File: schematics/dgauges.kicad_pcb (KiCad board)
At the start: 2 copper layers, 116 x 53.9 mm, 21 parts, among them J1 Conn_01x05_Female, U1 74HC595N, U2 74HC595N, U3 74HC595N, U4 74HC595N, U5 74HC595N

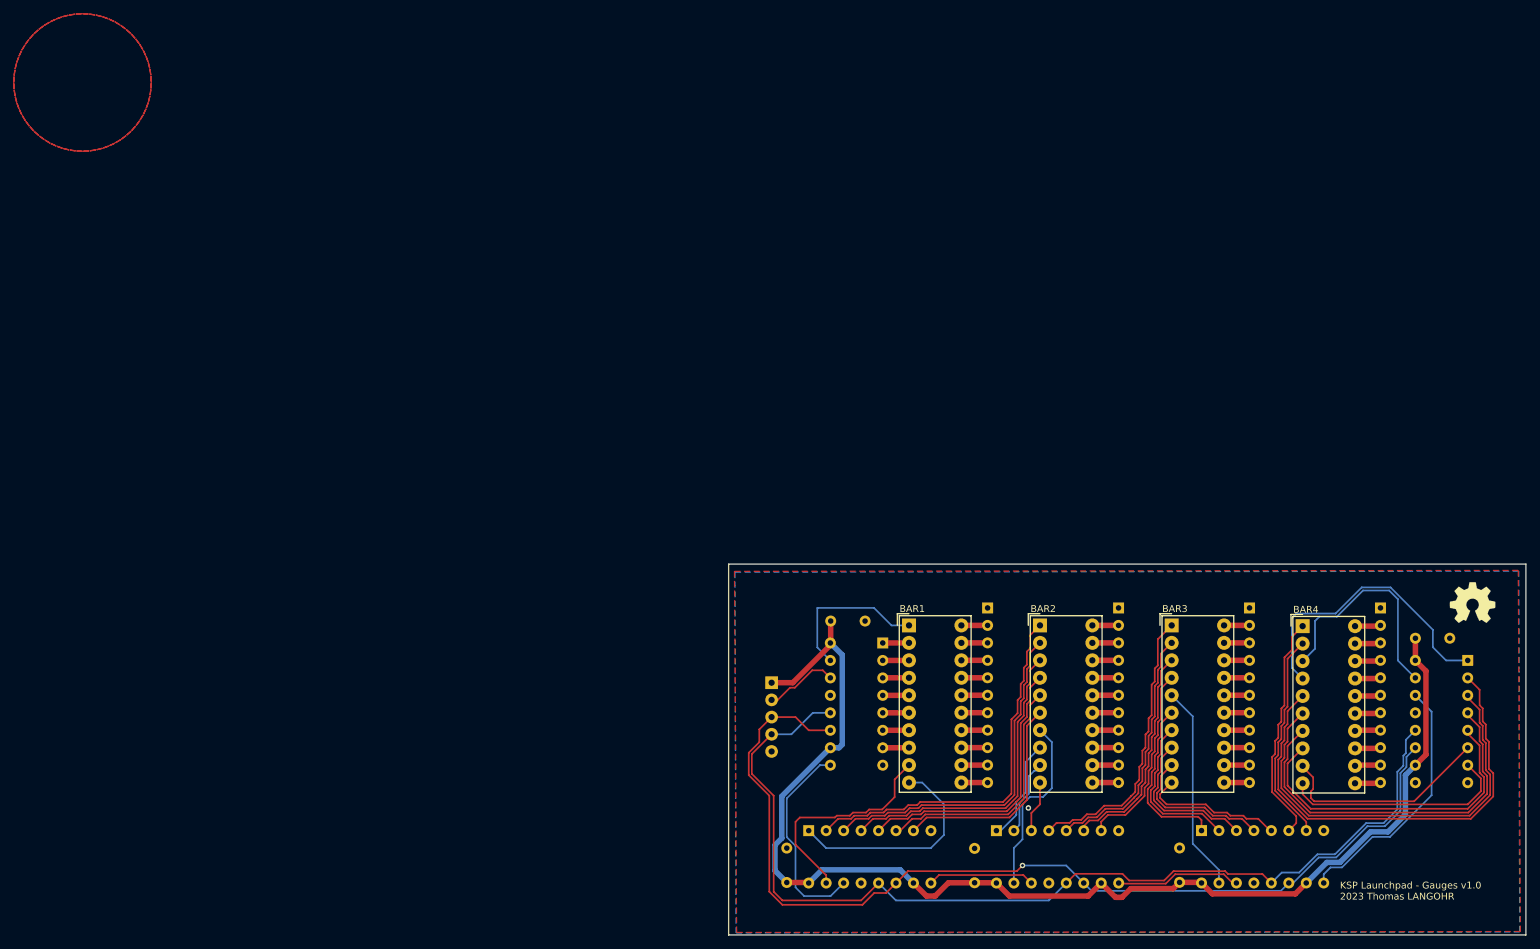
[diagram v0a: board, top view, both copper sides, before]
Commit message: SCH: mv sch to root dir / dgauges: GND plane filling, via stiching
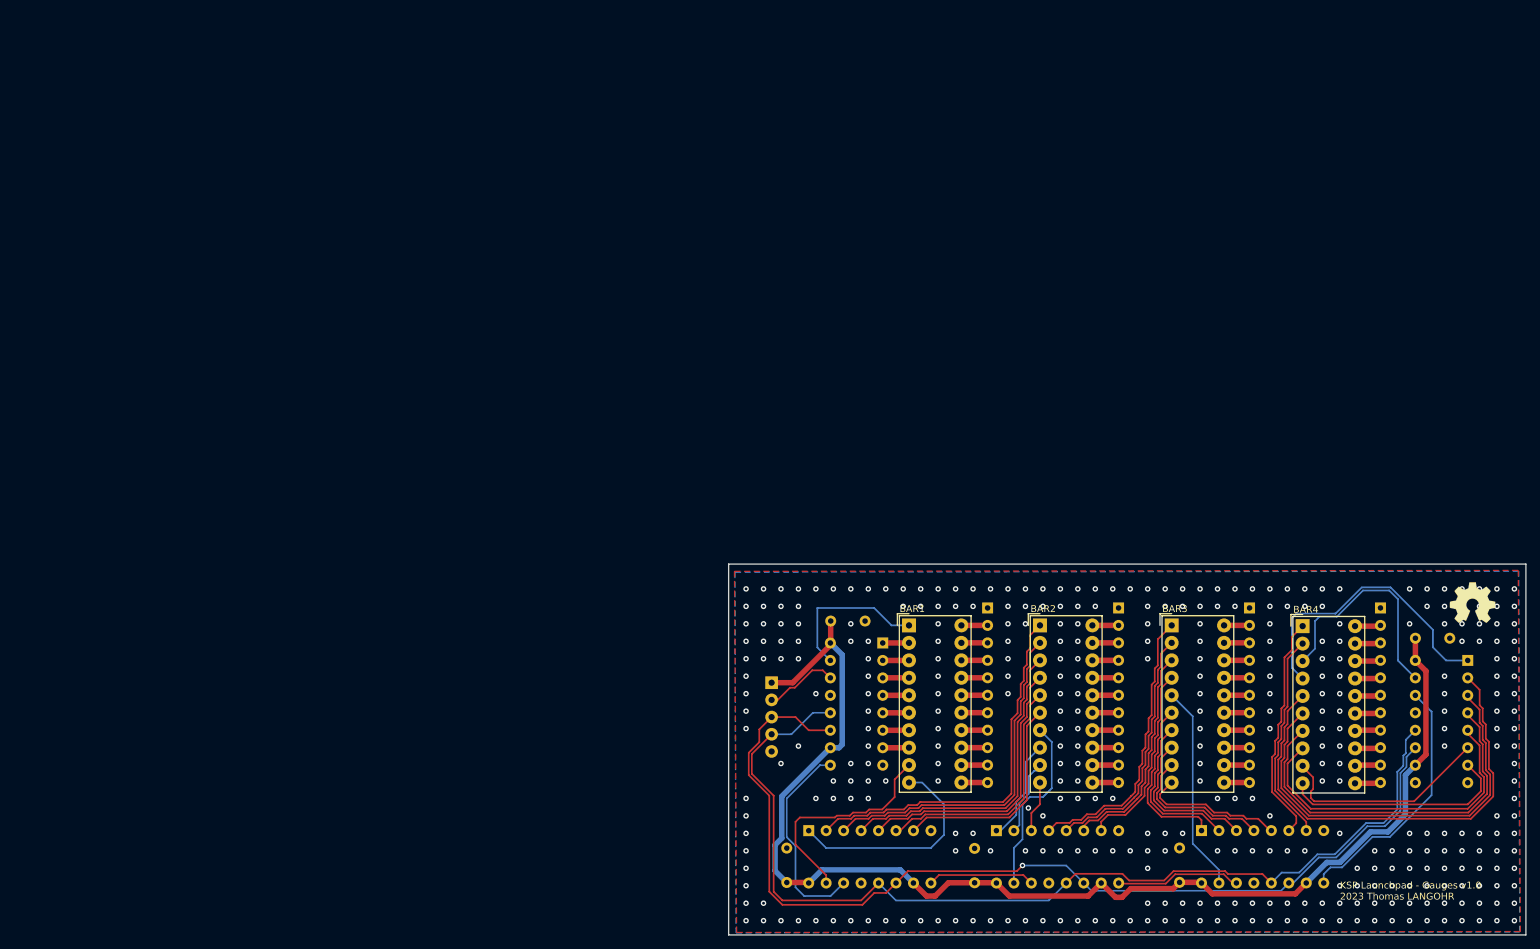
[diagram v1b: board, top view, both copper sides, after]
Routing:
- net GND: vias 1 -> 364
- removed copper zone on F.Cu, net (none)
